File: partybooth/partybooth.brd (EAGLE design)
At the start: 61.6 x 39 mm, 26 parts, among them IC1 TINY13-20PU, IC2 78L05Z, J1 Lamp, J2 Button, J3 12V, T1 2N3904, T2 2N3904, X1 1501_06

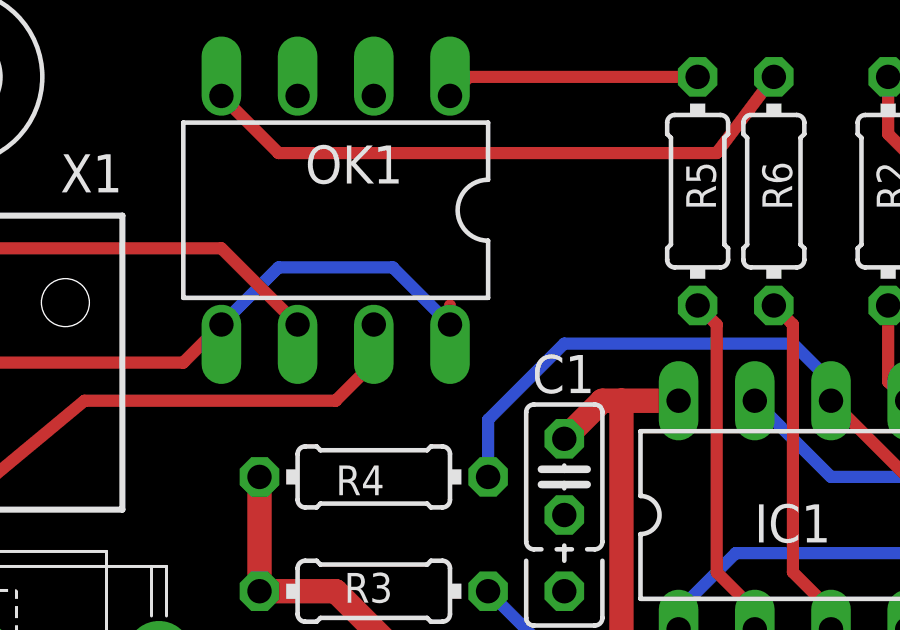
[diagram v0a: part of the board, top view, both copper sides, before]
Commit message: 
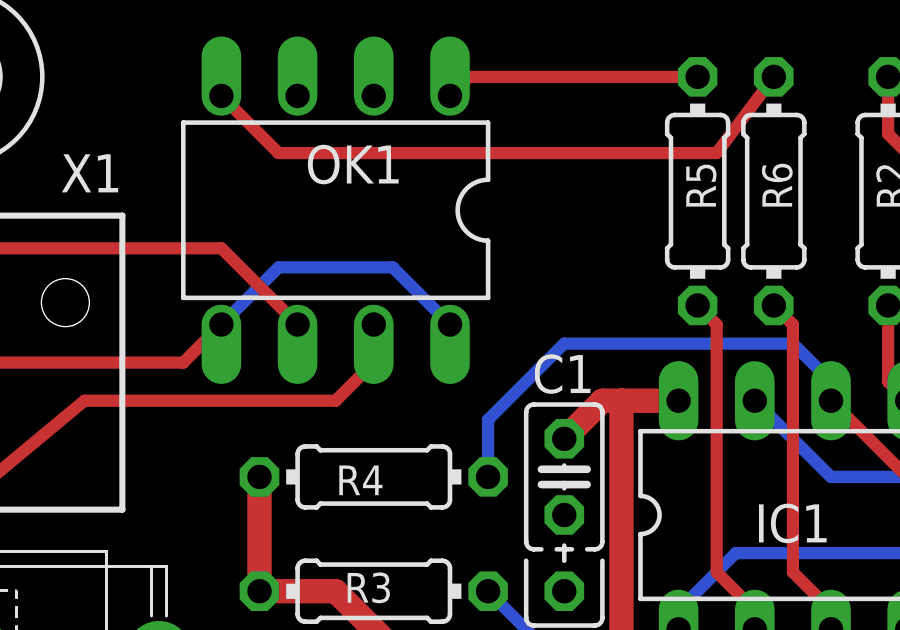
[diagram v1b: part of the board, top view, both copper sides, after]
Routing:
- net N$10: track 21.4 -> 20.8 mm
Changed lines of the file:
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@@
 <layer number="23" name="tOrigins" color="15" fill="1" visible="no" active="yes"/>
 <layer number="24" name="bOrigins" color="15" fill="1" visible="no" active="yes"/>
-<layer number="25" name="tNames" color="7" fill="1" visible="yes" active="yes"/>
-<layer number="26" name="bNames" color="7" fill="1" visible="yes" active="yes"/>
+<layer number="25" name="tNames" color="7" fill="1" visible="no" active="yes"/>
+<layer number="26" name="bNames" color="7" fill="1" visible="no" active="yes"/>
 <layer number="27" name="tValues" color="7" fill="1" visible="no" active="yes"/>
 <layer number="28" name="bValues" color="7" fill="1" visible="no" active="yes"/>
@@
 <contactref element="X1" pad="1"/>
 <contactref element="OK1" pad="8"/>
-<wire x1="20.32" y1="27.305" x2="20.32" y2="26.67" width="0.4064" layer="1"/>
 <wire x1="12.7" y1="26.67" x2="14.605" y2="28.575" width="0.4064" layer="16"/>
 <wire x1="14.605" y1="28.575" x2="18.415" y2="28.575" width="0.4064" layer="16"/>

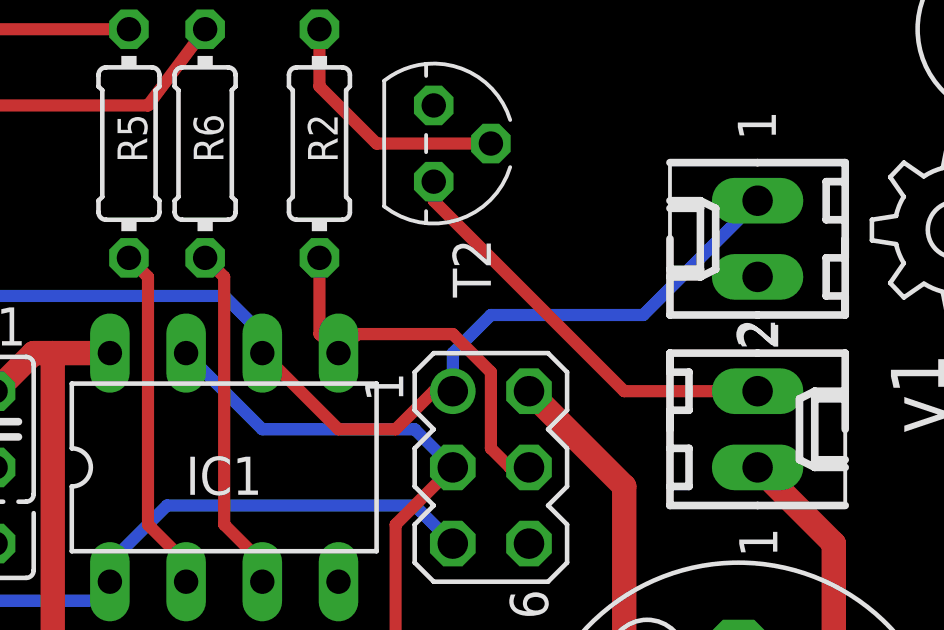
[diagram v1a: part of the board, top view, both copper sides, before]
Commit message: 
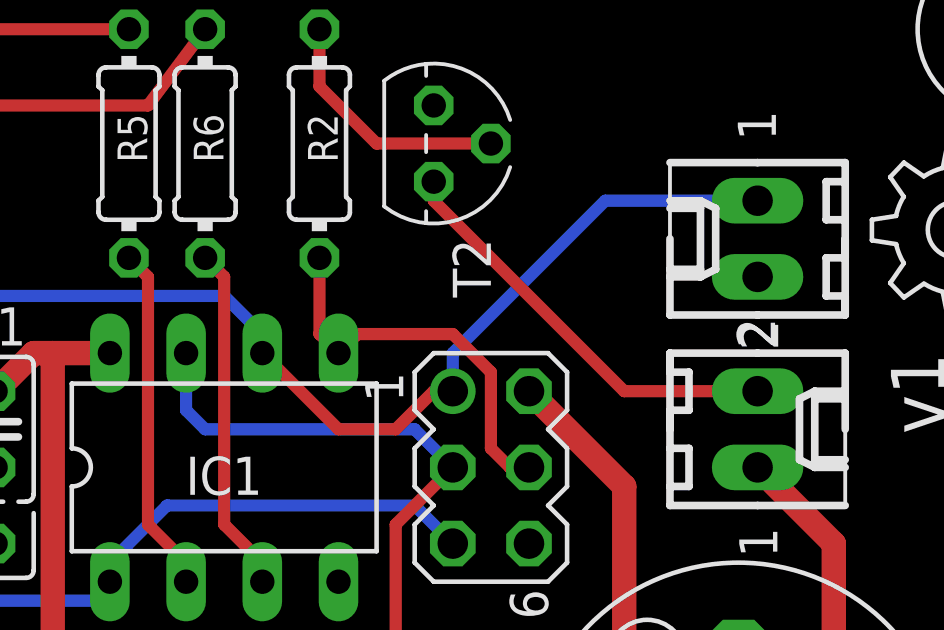
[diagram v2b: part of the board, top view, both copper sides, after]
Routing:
- net BZZ: track 18.5 -> 19.6 mm
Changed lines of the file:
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@@
 <contactref element="IC1" pad="7"/>
 <contactref element="SV1" pad="3"/>
-<wire x1="30.48" y1="24.13" x2="33.02" y2="21.59" width="0.4064" layer="16"/>
-<wire x1="33.02" y1="21.59" x2="38.1" y2="21.59" width="0.4064" layer="16"/>
+<wire x1="30.48" y1="24.13" x2="30.48" y2="22.225" width="0.4064" layer="16"/>
+<wire x1="30.48" y1="22.225" x2="31.115" y2="21.59" width="0.4064" layer="16"/>
+<wire x1="31.115" y1="21.59" x2="38.1" y2="21.59" width="0.4064" layer="16"/>
 <wire x1="38.1" y1="21.59" x2="39.37" y2="20.32" width="0.4064" layer="16"/>
 <wire x1="39.37" y1="20.32" x2="37.465" y2="18.415" width="0.4064" layer="1"/>
@@
 <wire x1="37.465" y1="21.59" x2="38.735" y2="22.86" width="0.4064" layer="1"/>
 <wire x1="38.735" y1="22.86" x2="39.37" y2="22.86" width="0.4064" layer="1"/>
-<wire x1="49.53" y1="29.21" x2="45.72" y2="25.4" width="0.4064" layer="16"/>
-<wire x1="45.72" y1="25.4" x2="40.64" y2="25.4" width="0.4064" layer="16"/>
-<wire x1="40.64" y1="25.4" x2="39.37" y2="24.13" width="0.4064" layer="16"/>
+<wire x1="49.53" y1="29.21" x2="44.45" y2="29.21" width="0.4064" layer="16"/>
+<wire x1="44.45" y1="29.21" x2="39.37" y2="24.13" width="0.4064" layer="16"/>
 <wire x1="39.37" y1="24.13" x2="39.37" y2="22.86" width="0.4064" layer="16"/>
 <wire x1="21.59" y1="21.59" x2="21.59" y2="23.495" width="0.4064" layer="16"/>

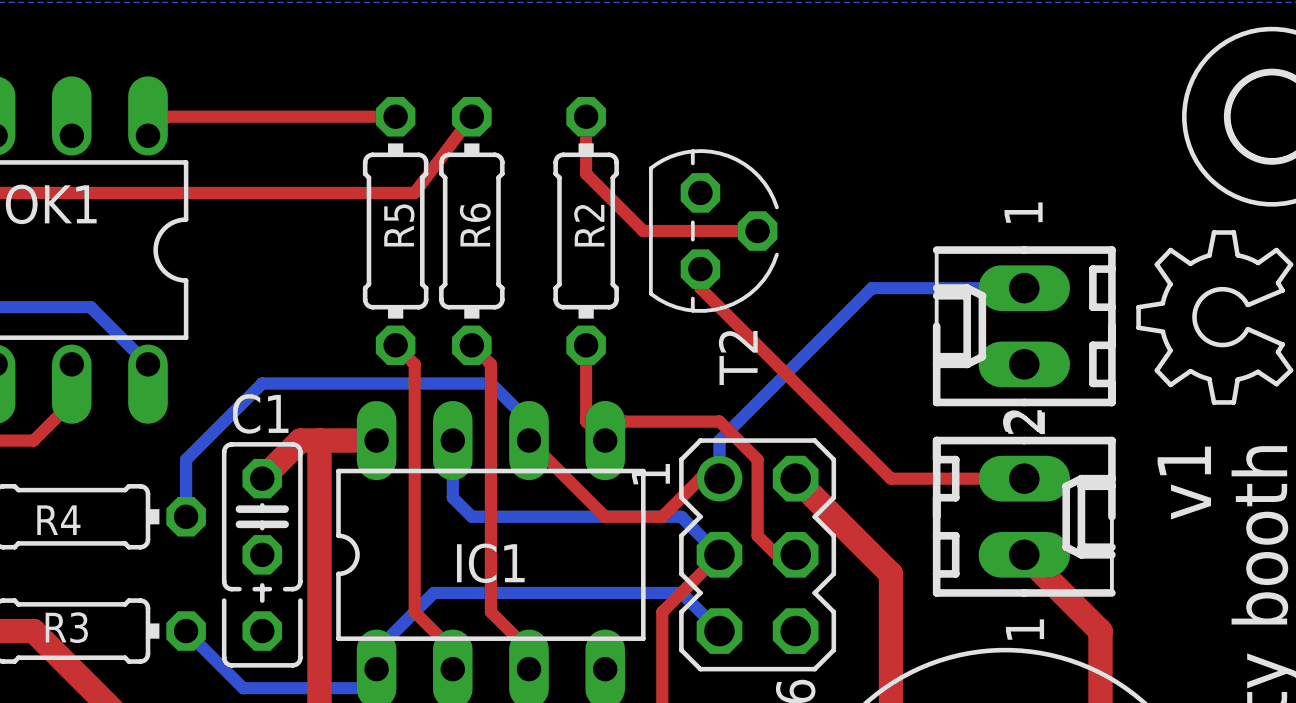
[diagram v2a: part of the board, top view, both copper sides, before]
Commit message: 
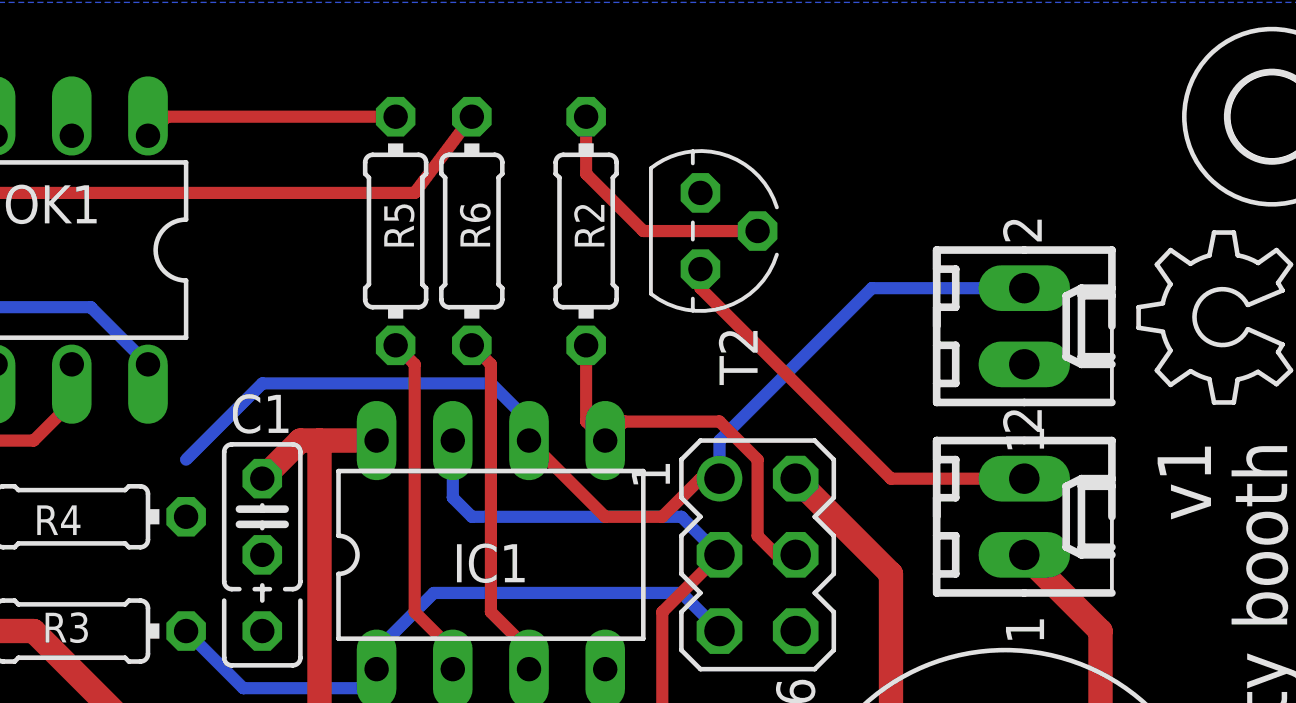
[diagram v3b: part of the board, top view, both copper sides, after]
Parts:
- turned J2 to 270 degrees
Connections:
- net BTN: now also J2.2; no longer J2.1
- net GND: now also J2.1; no longer J2.2
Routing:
- net BTN: track 37.0 -> 35.1 mm
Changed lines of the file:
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@@
 <layer number="17" name="Pads" color="2" fill="1" visible="yes" active="yes"/>
 <layer number="18" name="Vias" color="2" fill="1" visible="yes" active="yes"/>
-<layer number="19" name="Unrouted" color="6" fill="1" visible="no" active="yes"/>
+<layer number="19" name="Unrouted" color="6" fill="1" visible="yes" active="yes"/>
 <layer number="20" name="Dimension" color="15" fill="1" visible="yes" active="yes"/>
 <layer number="21" name="tPlace" color="7" fill="1" visible="yes" active="yes"/>
@@
 <attribute name="VALUE" x="20.066" y="31.115" size="1.27" layer="27" ratio="10" rot="R180"/>
 </element>
-<element name="J2" library="con-molex" package="6410-02" value="Button" x="49.53" y="27.94" smashed="yes" rot="R90">
-<attribute name="OC_NEWARK" value="unknown" x="83.82" y="45.72" size="1.778" layer="27" rot="R90" display="off"/>
-<attribute name="MPN" value="" x="83.82" y="45.72" size="1.778" layer="27" rot="R90" display="off"/>
-<attribute name="MF" value="" x="83.82" y="45.72" size="1.778" layer="27" rot="R90" display="off"/>
-<attribute name="OC_FARNELL" value="unknown" x="83.82" y="45.72" size="1.778" layer="27" rot="R90" display="off"/>
-<attribute name="VALUE" x="45.8739" y="26.0619" size="0.8128" layer="27" ratio="10" rot="R90"/>
+<element name="J2" library="con-molex" package="6410-02" value="Button" x="49.53" y="27.94" smashed="yes" rot="R270">
+<attribute name="OC_NEWARK" value="unknown" x="15.24" y="10.16" size="1.778" layer="27" rot="R270" display="off"/>
+<attribute name="MPN" value="" x="15.24" y="10.16" size="1.778" layer="27" rot="R270" display="off"/>
+<attribute name="MF" value="" x="15.24" y="10.16" size="1.778" layer="27" rot="R270" display="off"/>
+<attribute name="OC_FARNELL" value="unknown" x="15.24" y="10.16" size="1.778" layer="27" rot="R270" display="off"/>
+<attribute name="VALUE" x="53.1861" y="29.8181" size="0.8128" layer="27" ratio="10" rot="R270"/>
 </element>
 <element name="SV1" library="con-lstb" package="MA03-2" value="ICSP" x="40.64" y="20.32" smashed="yes" rot="R270">
@@
 <contactref element="C3" pad="-"/>
 <contactref element="IC2" pad="2"/>
-<contactref element="J2" pad="2"/>
 <contactref element="J3" pad="1"/>
 <polygon width="0.4064" layer="16">
@@
 <vertex x="0.635" y="0.635"/>
 </polygon>
+<contactref element="J2" pad="1"/>
 </signal>
 <signal name="+5V">
@@
 </signal>
 <signal name="BTN">
-<contactref element="R4" pad="1"/>
-<contactref element="J2" pad="1"/>
 <contactref element="IC1" pad="6"/>
 <contactref element="SV1" pad="1"/>
@@
 <wire x1="37.465" y1="21.59" x2="38.735" y2="22.86" width="0.4064" layer="1"/>
 <wire x1="38.735" y1="22.86" x2="39.37" y2="22.86" width="0.4064" layer="1"/>
-<wire x1="49.53" y1="29.21" x2="44.45" y2="29.21" width="0.4064" layer="16"/>
 <wire x1="44.45" y1="29.21" x2="39.37" y2="24.13" width="0.4064" layer="16"/>
 <wire x1="39.37" y1="24.13" x2="39.37" y2="22.86" width="0.4064" layer="16"/>
-<wire x1="21.59" y1="21.59" x2="21.59" y2="23.495" width="0.4064" layer="16"/>
 <wire x1="21.59" y1="23.495" x2="24.13" y2="26.035" width="0.4064" layer="16"/>
 <wire x1="24.13" y1="26.035" x2="31.75" y2="26.035" width="0.4064" layer="16"/>
 <wire x1="31.75" y1="26.035" x2="33.02" y2="24.765" width="0.4064" layer="16"/>
 <wire x1="33.02" y1="24.765" x2="33.02" y2="24.13" width="0.4064" layer="16"/>
+<contactref element="R4" pad="1"/>
+<contactref element="J2" pad="2"/>
+<wire x1="49.53" y1="29.21" x2="44.45" y2="29.21" width="0.4064" layer="16"/>
+<wire x1="21.59" y1="21.59" x2="21.59" y2="23.495" width="0" layer="19" extent="16-16"/>
 </signal>
 </signals>
